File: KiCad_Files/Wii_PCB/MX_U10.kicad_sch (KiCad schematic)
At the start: 8 parts, among them Y1 ABS06-107-32.768KHZ-T

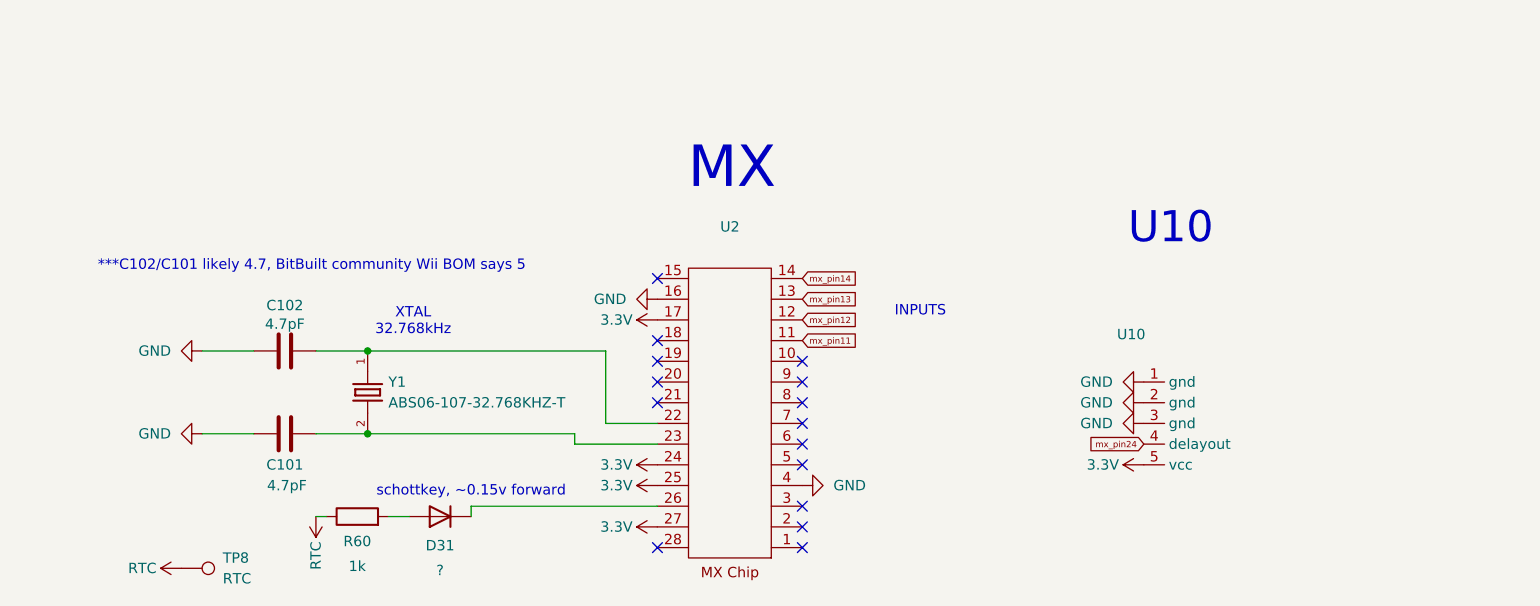
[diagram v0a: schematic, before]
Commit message: Updated RAM & GPU bus to allow custom net rules for measuring intra-track spacing, added pad for reset, removed debug pads, reorganized ram schematic to cluster length matched signals, changed MX chip and U10 symbols, and re-labeled the wifi net interface.
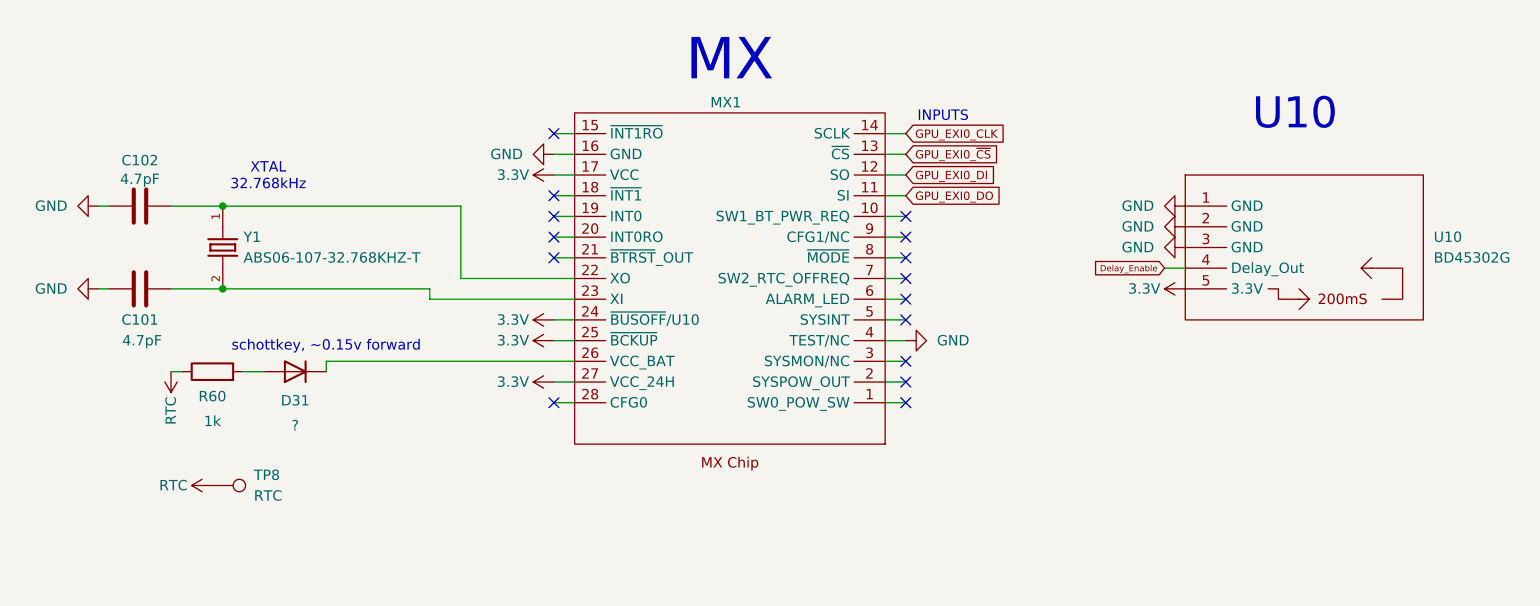
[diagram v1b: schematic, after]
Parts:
- removed U10: ~, Package_TO_SOT_SMD:SOT-23-5, symbol Wii_symbols:u10
- added U10: BD45302G, WeeWii_Library:u10, symbol Wii_symbols:U10
- MX1: renamed from U2; footprint wii_bgaLibrary:MX_SOIC -> WeeWii_Library:MX_SOIC
- Y1: footprint wii_bgaLibrary:Crystal_SMD_2012-2Pin_2.0x1.2mm -> WeeWii_Library:Crystal_SMD_2012-2Pin_2.0x1.2mm
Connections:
- net 3.3V: now also U10.5 (3.3V)
- net GND: now also U10.1 (GND), U10.2 (GND), U10.3 (GND)
- net mx_pin11 renamed GPU_EXI0_DO
- net mx_pin12 renamed GPU_EXI0_DI
- net mx_pin13 renamed GPU_EXI0_~{CS}
- net mx_pin14 renamed GPU_EXI0_CLK
- new net Delay_Enable: U10.4 (Delay_Out)
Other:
- note removed: "***C102/C101 likely 4.7, BitBuilt community Wii BOM says 5"
- moved on the sheet: C101, C102, D31, R60, TP8, Y1
